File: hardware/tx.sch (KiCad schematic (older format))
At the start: 63 parts, among them Q1 RE1C002UN, U1 ADF4158, U10 HMC431LP4, U12 PAT1220-6dB, U15 SMA, U17 SE5004L, U3 PAT1220-6dB, U7 TLV172DCK

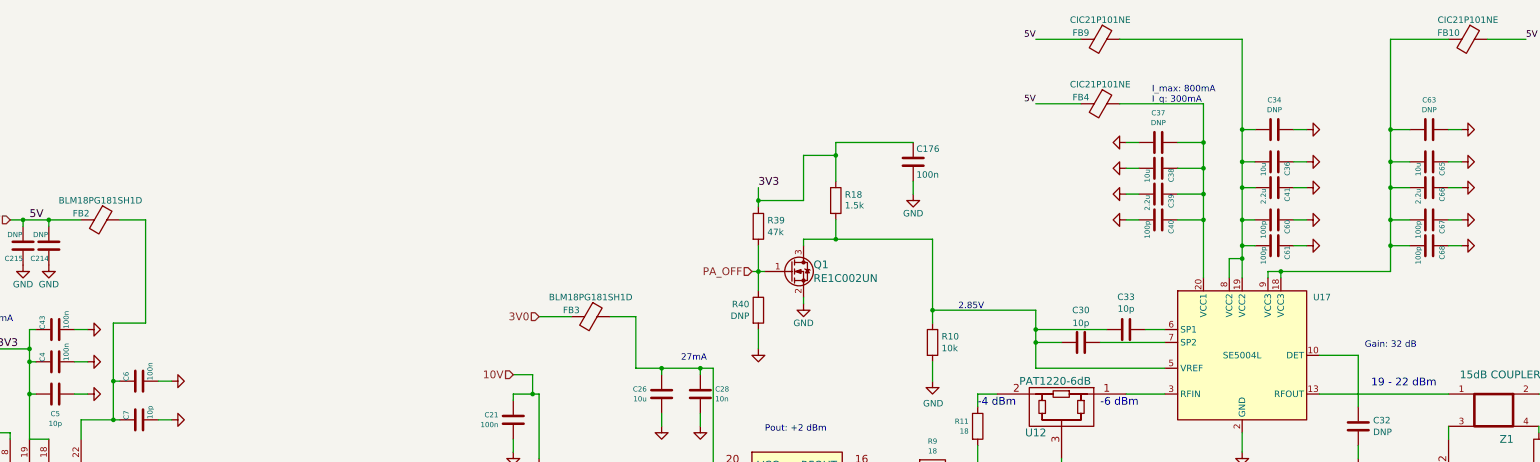
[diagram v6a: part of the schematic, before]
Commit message: Fixed ERC errors.
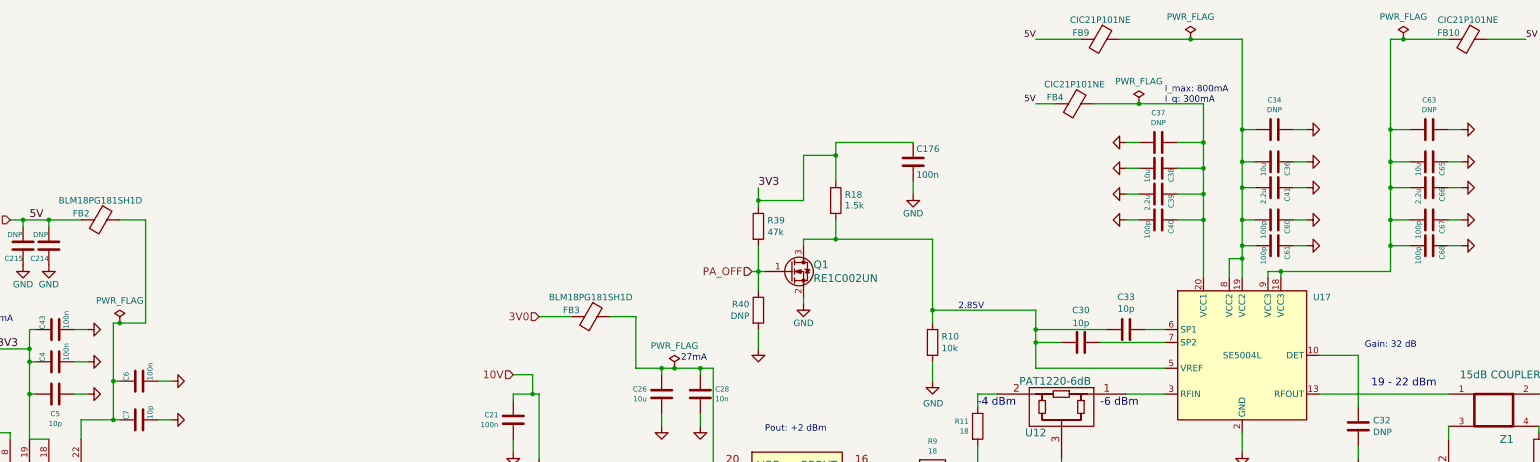
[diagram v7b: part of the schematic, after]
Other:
- moved on the sheet: FB4
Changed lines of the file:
@@
 	0    1    1    0
 $EndComp
-Text Label 11000 2750 2    50   ~ 0
-5V
 Text Notes 13550 4650 0    50   ~ 0
 Gain: 32 dB
@@
 Text Notes 2850 4450 0    50   ~ 0
 35 mA
-Text Notes 11900 2750 0    50   ~ 0
+Text Notes 12000 2750 0    50   ~ 0
 I_max: 800mA\nI_q: 300mA
 $Comp
@@
 Wire Wire Line
 	14900 5300 14900 5250
-Text HLabel 6950 4850 0    60   Input ~ 0
-10V
-Wire Wire Line
-	6950 4850 7100 4850
 Wire Wire Line
 	7100 4850 7100 5000
 Connection ~ 7100 5000
-Text HLabel 3050 3650 0    60   Input ~ 0
-5V
 Text HLabel 2750 4600 0    60   Input ~ 0
 3V3
@@
 $EndComp
 Wire Wire Line
-	3050 3650 3150 3650
-Wire Wire Line
 	3600 5200 3850 5200
-Wire Wire Line
-	4100 4450 3850 4450
 Wire Wire Line
 	4100 3650 4100 4450
@@
 L Device:Ferrite_Bead FB4
 U 1 1 59758907
-P 11500 2750
-F 0 "FB4" V 11450 2600 50  0000 C CNN
-F 1 "CIC21P101NE" V 11350 2750 50  0000 C CNN
-F 2 "Inductor_SMD:L_0805_2012Metric" H 11500 2750 60  0001 C CNN
-F 3 "" H 11500 2750 60  0000 C CNN
-F 4 "CIC21P101NE" H 0   0   50  0001 C CNN "MFN"
-	1    11500 2750
+P 11300 2750
+F 0 "FB4" V 11250 2600 50  0000 C CNN
+F 1 "CIC21P101NE" V 11150 2750 50  0000 C CNN
+F 2 "Inductor_SMD:L_0805_2012Metric" H 11300 2750 60  0001 C CNN
+F 3 "" H 11300 2750 60  0000 C CNN
+F 4 "CIC21P101NE" H -200 0   50  0001 C CNN "MFN"
+	1    11300 2750
 	0    1    1    0
 $EndComp
@@
 	2800 4750 2950 4750
 Wire Wire Line
-	8100 4800 8400 4800
+	8100 4800 8200 4800
 Wire Wire Line
 	3850 4900 3850 5200
@@
 	7700 4400 7900 4400
 Wire Wire Line
-	11000 2750 11350 2750
-Wire Wire Line
-	11650 2750 12300 2750
+	11450 2750 11800 2750
 Wire Wire Line
 	4600 6950 4600 7000
@@
 	1    0    0    -1
 $EndComp
-Text Label 3200 3650 0    60   ~ 0
-5V
 $Comp
 L Device:C C30
@@
 	12600 4100 12600 3950
 Wire Wire Line
-	12600 2250 11650 2250
-Text Label 11000 2250 2    50   ~ 0
-5V
+	12600 2250 12200 2250
 $Comp
 L Device:Ferrite_Bead FB9
@@
 $EndComp
 Wire Wire Line
-	11350 2250 11000 2250
-Wire Wire Line
 	12500 4100 12500 3950
 Wire Wire Line
@@
 	13750 4050 13750 3850
 Wire Wire Line
-	13750 2250 14200 2250
-Text Label 14800 2250 0    50   ~ 0
-5V
+	13750 2250 13850 2250
 $Comp
 L Device:Ferrite_Bead FB10
@@
 Wire Wire Line
 	15550 5300 15550 5200
+Wire Wire Line
+	6950 4850 7100 4850
+Text HLabel 6950 4850 0    60   Input ~ 0
+10V
+Wire Wire Line
+	4100 4450 3900 4450
+Text Label 14800 2250 0    50   ~ 0
+5V
+Wire Wire Line
+	11000 2750 11150 2750
+Text Label 11000 2750 2    50   ~ 0
+5V
+Wire Wire Line
+	11350 2250 11000 2250
+Text Label 11000 2250 2    50   ~ 0
+5V
+Text Label 3200 3650 0    60   ~ 0
+5V
+Wire Wire Line
+	3050 3650 3150 3650
+Text HLabel 3050 3650 0    60   Input ~ 0
+5V
+$Comp
+L power:PWR_FLAG #FLG0105
+U 1 1 5CF1FD67
+P 3900 4450
+F 0 "#FLG0105" H 3900 4525 50  0001 C CNN
+F 1 "PWR_FLAG" H 3900 4624 50  0000 C CNN
+F 2 "" H 3900 4450 50  0001 C CNN
+F 3 "~" H 3900 4450 50  0001 C CNN
+	1    3900 4450
+	1    0    0    -1
+$EndComp
+Connection ~ 3900 4450
+Wire Wire Line
+	3900 4450 3850 4450
+$Comp
+L power:PWR_FLAG #FLG0106
+U 1 1 5CF1FF83
+P 8200 4800
+F 0 "#FLG0106" H 8200 4875 50  0001 C CNN
+F 1 "PWR_FLAG" H 8200 4974 50  0000 C CNN
+F 2 "" H 8200 4800 50  0001 C CNN
+F 3 "~" H 8200 4800 50  0001 C CNN
+	1    8200 4800
+	1    0    0    -1
+$EndComp
+Connection ~ 8200 4800
+Wire Wire Line
+	8200 4800 8400 4800
+$Comp
+L power:PWR_FLAG #FLG0107
+U 1 1 5CF21675
+P 12200 2250
+F 0 "#FLG0107" H 12200 2325 50  0001 C CNN
+F 1 "PWR_FLAG" H 12200 2424 50  0000 C CNN
+F 2 "" H 12200 2250 50  0001 C CNN
+F 3 "~" H 12200 2250 50  0001 C CNN
+	1    12200 2250
+	1    0    0    -1
+$EndComp
+Connection ~ 12200 2250
+Wire Wire Line
+	12200 2250 11650 2250
+$Comp
+L power:PWR_FLAG #FLG0108
+U 1 1 5CF21707
+P 13850 2250
+F 0 "#FLG0108" H 13850 2325 50  0001 C CNN
+F 1 "PWR_FLAG" H 13850 2424 50  0000 C CNN
+F 2 "" H 13850 2250 50  0001 C CNN
+F 3 "~" H 13850 2250 50  0001 C CNN
+	1    13850 2250
+	1    0    0    -1
+$EndComp
+Connection ~ 13850 2250
+Wire Wire Line
+	13850 2250 14200 2250
+$Comp
+L power:PWR_FLAG #FLG0109
+U 1 1 5CF2E52E
+P 11800 2750
+F 0 "#FLG0109" H 11800 2825 50  0001 C CNN
+F 1 "PWR_FLAG" H 11800 2924 50  0000 C CNN
+F 2 "" H 11800 2750 50  0001 C CNN
+F 3 "~" H 11800 2750 50  0001 C CNN
+	1    11800 2750
+	1    0    0    -1
+$EndComp
+Connection ~ 11800 2750
+Wire Wire Line
+	11800 2750 12300 2750
 $EndSCHEMATC

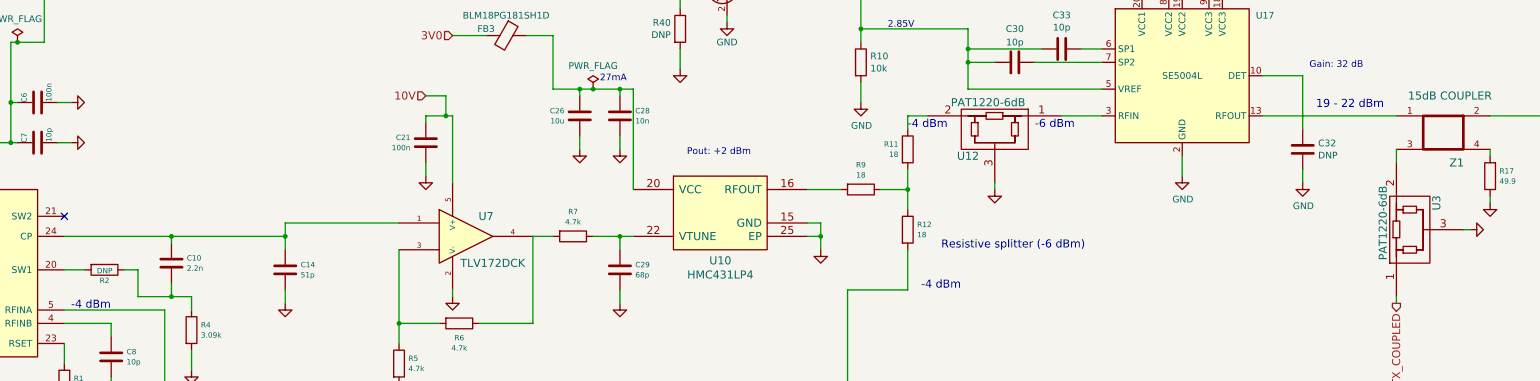
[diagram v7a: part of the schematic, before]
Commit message: Improved documentation and added schematics to default libraries.
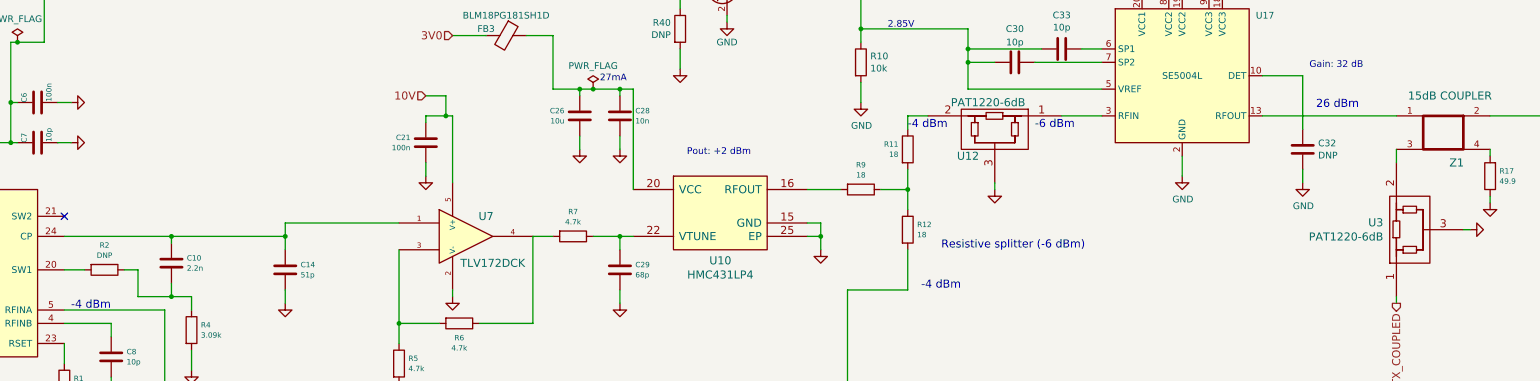
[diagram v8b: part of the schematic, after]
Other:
- note added: "26 dBm"
- note removed: "19 - 22 dBm"
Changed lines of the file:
@@
 U 1 1 54FACF33
 P 4550 6150
-F 0 "R2" V 4630 6150 40  0000 C CNN
-F 1 "DNP" V 4557 6151 40  0000 C CNN
+F 0 "R2" V 4366 6150 40  0000 C CNN
+F 1 "DNP" V 4442 6150 40  0000 C CNN
 F 2 "Resistor_SMD:R_0402_1005Metric" V 4480 6150 30  0001 C CNN
 F 3 "" H 4550 6150 30  0000 C CNN
@@
 Gain: 32 dB
 Text Notes 13600 4950 0    60   ~ 0
-19 - 22 dBm
+26 dBm
 $Comp
 L power:GND #PWR0110
@@
 U 1 1 551D3333
 P 14200 5850
-F 0 "U3" H 14400 5550 60  0000 C CNN
-F 1 "PAT1220-6dB" H 14250 5950 60  0000 C CNN
+F 0 "U3" V 14253 5948 60  0000 L CNN
+F 1 "PAT1220-6dB" V 14147 5948 60  0000 L CNN
 F 2 "fmcw:PAT1220" H 14200 5850 60  0001 C CNN
 F 3 "" H 14200 5850 60  0000 C CNN
